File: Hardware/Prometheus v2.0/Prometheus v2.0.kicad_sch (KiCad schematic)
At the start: 21 parts, among them K1 Relay_SPDT, Q1 IRLML6246, Q2 IRLML6246, Q3 IRLML6246, SW1 SW_Push, U1 LMS1585ACT-3.3_NOPB, U2 LM7805_TO220

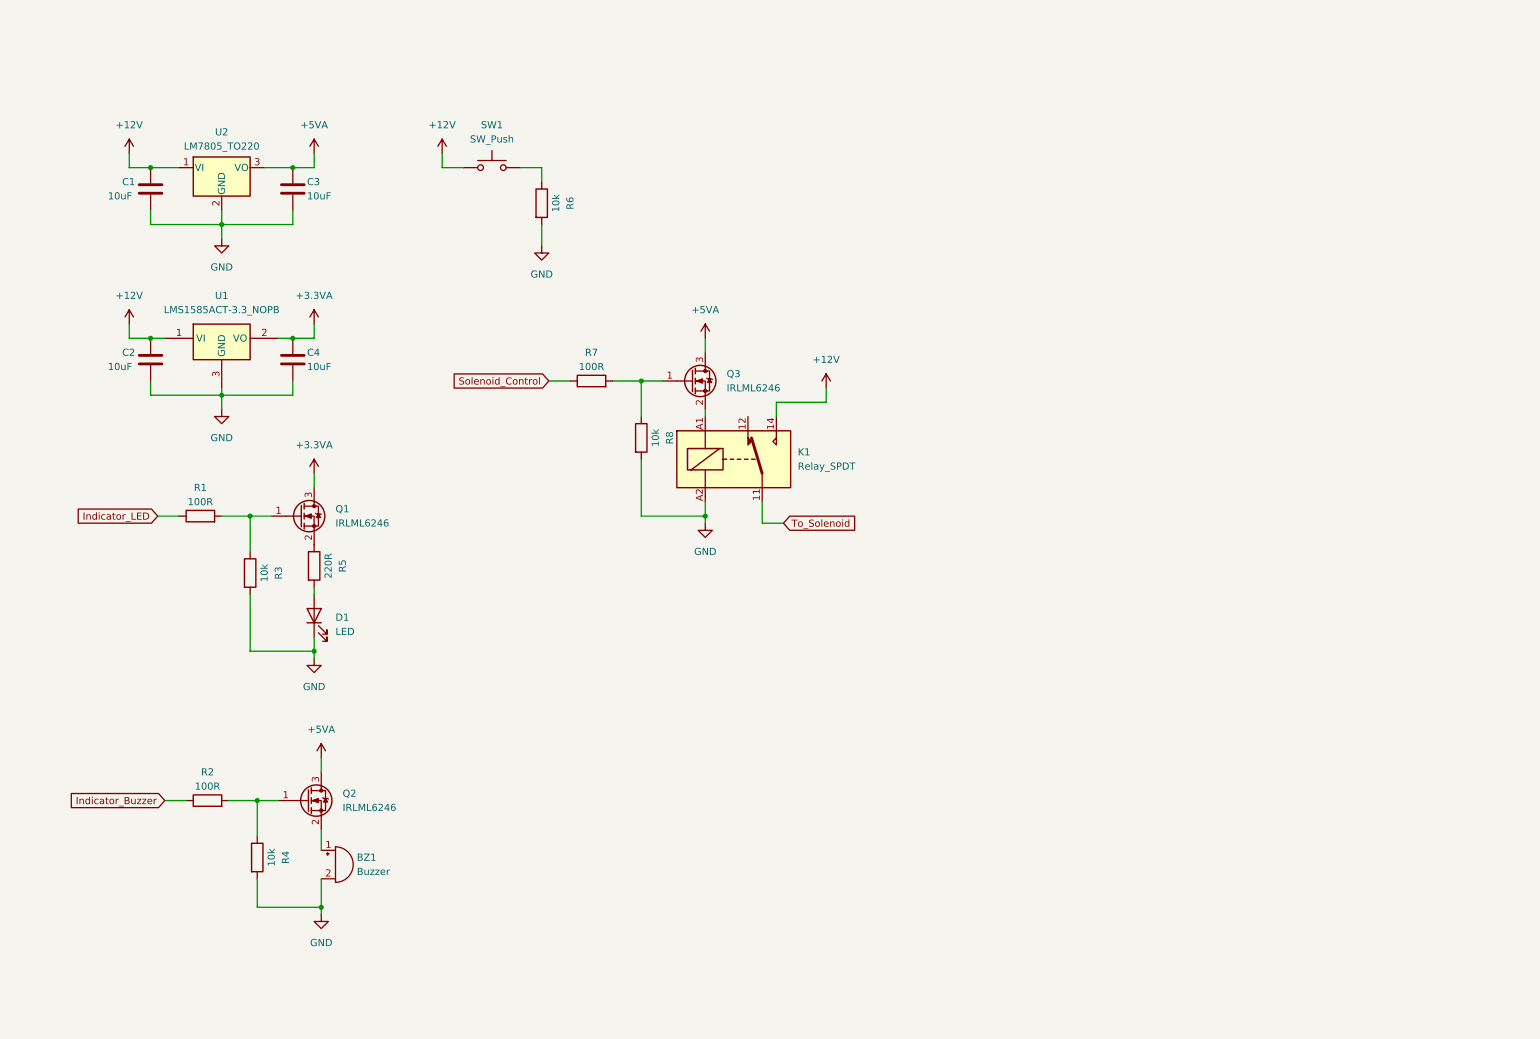
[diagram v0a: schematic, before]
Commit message: v1.0 - Phase 2
- Completed the complete schematic
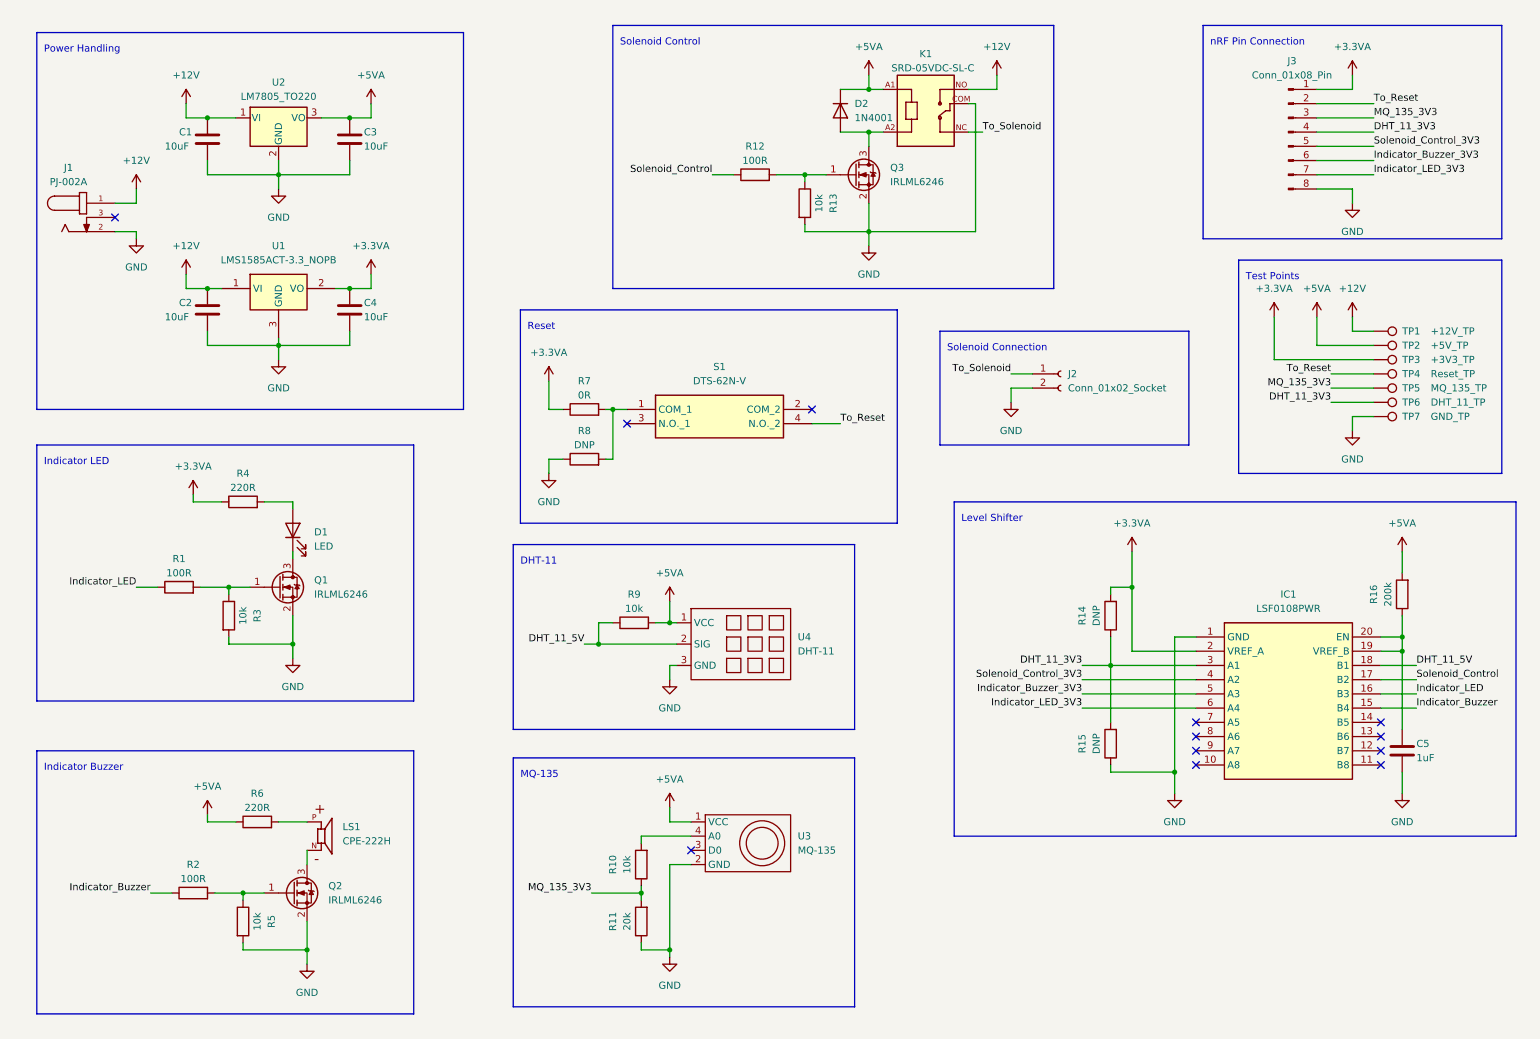
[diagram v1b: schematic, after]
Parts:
- removed BZ1: Buzzer, symbol Device:Buzzer
- removed K1: Relay_SPDT, symbol Relay:Relay_SPDT
- removed SW1: SW_Push, symbol Switch:SW_Push
- added C5: 1uF, symbol Device:C
- added D2: 1N4001, Diode_THT:D_DO-41_SOD81_P10.16mm_Horizontal, symbol Diode:1N4001
- added IC1: LSF0108PWR, SOP65P640X120-20N, symbol Level Shifter:LSF0108PWR
- added J1: PJ-002A, PJ-002A:CUI_PJ-002A, symbol Connectors:PJ-002A
- added J2: Conn_01x02_Socket, symbol Connector:Conn_01x02_Socket
- added J3: Conn_01x08_Pin, symbol Connector:Conn_01x08_Pin
- added K1: SRD-05VDC-SL-C, SRD-05VDC-SL-C:RELAY_SRD-05VDC-SL-C, symbol Mechanical Relays:SRD-05VDC-SL-C
- added LS1: CPE-222H, CPE-222H:CUI_CPE-222H, symbol Piezzo Electric Buzzer:CPE-222H
- added R10, R9: 10k, symbol Device:R
- added R11: 20k, symbol Device:R
- added R14, R15, R8: DNP, symbol Device:R
- added R16: 200k, symbol Device:R
- added R7: 0R, symbol Device:R
- added S1: DTS-62N-V, DTS62NV, symbol Tactile Switch:DTS-62N-V
- added TP1: +12V_TP, symbol Connector:TestPoint
- added TP2: +5V_TP, symbol Connector:TestPoint
- added TP3: +3V3_TP, symbol Connector:TestPoint
- added TP4: Reset_TP, symbol Connector:TestPoint
- added TP5: MQ_135_TP, symbol Connector:TestPoint
- added TP6: DHT_11_TP, symbol Connector:TestPoint
- added TP7: GND_TP, symbol Connector:TestPoint
- added U3: MQ-135, symbol Sensors:MQ-135
- added U4: DHT-11, symbol Sensors:DHT-11
- R4, R6: value 10k -> 220R
- R5: value 220R -> 10k
- renumbered R7 to R12, R8 to R13
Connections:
- net +12V: now also J1.1, K1.NO, TP1.1
- net +3.3VA: now also R4.1, IC1.2 (VREF_A), J3.1 (Pin_1), R14.2, R7.1, TP3.1; no longer Q1.3 (D)
- net +5VA: now also R6.1, D2.1 (K), K1.A1, R16.2, R9.2, TP2.1, U3.1 (VCC), U4.1 (VCC); no longer Q2.3 (D), Q3.3 (D)
- net GND: now also Q1.2 (S), Q2.2 (S), Q3.2 (S), R5.2, C5.2, IC1.1 (GND), J1.2, J2.2 (Pin_2), J3.8 (Pin_8), K1.COM, R11.1, R15.1, R8.1, TP7.1, U3.2 (GND), U4.3 (GND); no longer D1.1 (K), R4.2, R6.2
- net Indicator_Buzzer: now also IC1.15 (B4)
- net Indicator_LED: now also IC1.16 (B3)
- net Solenoid_Control: now also IC1.17 (B2)
- net To_Solenoid: now also J2.1 (Pin_1), K1.NC
- net at R5.1: now also Q2.1 (G), R2.2; no longer Q1.2 (S)
- net at D1.2 (A): now also R4.2; no longer R5.2
- new net: LS1.N, Q2.3 (D)
- new net: LS1.P, R6.2
- new net: R7.2, R8.2, S1.1 (COM_1)
- new net: D1.1 (K), Q1.3 (D)
- new net: D2.2 (A), K1.A2, Q3.3 (D)
- new net: C5.1, IC1.19 (VREF_B), IC1.20 (EN), R16.1
- new net: R10.2, U3.4 (A0)
- new net DHT_11_3V3: IC1.3 (A1), J3.4 (Pin_4), R14.1, R15.2, TP6.1
- new net DHT_11_5V: IC1.18 (B1), R9.1, U4.2 (SIG)
- new net Indicator_Buzzer_3V3: IC1.5 (A3), J3.6 (Pin_6)
- new net Indicator_LED_3V3: IC1.6 (A4), J3.7 (Pin_7)
- new net MQ_135_3V3: J3.3 (Pin_3), R10.1, R11.2, TP5.1
- new net Solenoid_Control_3V3: IC1.4 (A2), J3.5 (Pin_5)
- new net To_Reset: J3.2 (Pin_2), S1.4 (N.O._2), TP4.1
- no-connect marks 0 -> 12
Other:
- note added: "DHT-11"
- note added: "Indicator Buzzer"
- note added: "Indicator LED"
- note added: "Level Shifter"
- note added: "MQ-135"
- note added: "Power Handling"
- note added: "Reset"
- note added: "Solenoid Connection"
- note added: "Solenoid Control"
- note added: "Test Points"
- note added: "nRF Pin Connection"
- company: (none) -> Asanka Sovis
- title: (none) -> Prometheus Main PCB v2.0
- moved on the sheet: C1, C2, C3, C4, Q1, Q3, R1, R12, R13, R3, U1, U2

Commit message: v2.1
- First design completion
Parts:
- removed C5: 1uF, symbol Device:C
- removed J3: Conn_01x08_Pin, symbol Connector:Conn_01x08_Pin
- removed R11: 20k, symbol Device:R
- removed R16: 200k, symbol Device:R
- removed R9: 10k, symbol Device:R
- removed TP1: +12V_TP, symbol Connector:TestPoint
- removed TP2: +5V_TP, symbol Connector:TestPoint
- removed TP3: +3V3_TP, symbol Connector:TestPoint
- removed TP4: Reset_TP, symbol Connector:TestPoint
- removed TP5: MQ_135_TP, symbol Connector:TestPoint
- removed TP6: DHT_11_TP, symbol Connector:TestPoint
- removed TP7: GND_TP, symbol Connector:TestPoint
- removed U3: MQ-135, symbol Sensors:MQ-135
- removed U4: DHT-11, symbol Sensors:DHT-11
- added C3, C7: 0.1uF, Capacitor_SMD:C_0805_2012Metric, symbol Device:C
- added C6: 1uF, Capacitor_SMD:C_0805_2012Metric, symbol Device:C
- added J3: Conn_01x12_Pin, Connector_PinHeader_2.54mm:PinHeader_1x12_P2.54mm_Horizontal, symbol Connector:Conn_01x12_Pin
- added R12, R2, R21: 10k, Resistor_SMD:R_0805_2012Metric, symbol Device:R
- added R3: 20k, Resistor_SMD:R_0805_2012Metric, symbol Device:R
- added R5, R6: DNP, Resistor_SMD:R_0805_2012Metric, symbol Device:R
- added R7: 2k, Resistor_SMD:R_0805_2012Metric, symbol Device:R
- added R8: 200k, Resistor_SMD:R_0805_2012Metric, symbol Device:R
- added TP1: 12V_TP, TestPoint:TestPoint_Pad_1.0x1.0mm, symbol Connector:TestPoint_Small
- added TP10: MQ_135_SDA_TP, TestPoint:TestPoint_Pad_1.0x1.0mm, symbol Connector:TestPoint_Small
- added TP11: MQ_135_5V_TP, TestPoint:TestPoint_Pad_1.0x1.0mm, symbol Connector:TestPoint_Small
- added TP12: MQ_135_D_TP, TestPoint:TestPoint_Pad_1.0x1.0mm, symbol Connector:TestPoint_Small
- added TP13: Solenoid_Out_TP, TestPoint:TestPoint_Pad_1.0x1.0mm, symbol Connector:TestPoint_Small
- added TP14: LED_TP, TestPoint:TestPoint_Pad_1.0x1.0mm, symbol Connector:TestPoint_Small
- added TP15: Buzzer_TP, TestPoint:TestPoint_Pad_1.0x1.0mm, symbol Connector:TestPoint_Small
- added TP16: Solenoid_Control_3V3_TP, TestPoint:TestPoint_Pad_1.0x1.0mm, symbol Connector:TestPoint_Small
- added TP17: Indicator_Buzzer_3V3_TP, TestPoint:TestPoint_Pad_1.0x1.0mm, symbol Connector:TestPoint_Small
- added TP18: Indicator_LED_3V3_TP, TestPoint:TestPoint_Pad_1.0x1.0mm, symbol Connector:TestPoint_Small
- added TP19: DHT_11_3V3_TP, TestPoint:TestPoint_Pad_1.0x1.0mm, symbol Connector:TestPoint_Small
- added TP2: MQ_135_A_3V3_TP, TestPoint:TestPoint_Pad_1.0x1.0mm, symbol Connector:TestPoint_Small
- added TP20: MQ_135_SDA_3V3_TP, TestPoint:TestPoint_Pad_1.0x1.0mm, symbol Connector:TestPoint_Small
- added TP21: MQ_135_SCL_3V3_TP, TestPoint:TestPoint_Pad_1.0x1.0mm, symbol Connector:TestPoint_Small
- added TP22: MQ_135_CS_3V3_TP, TestPoint:TestPoint_Pad_1.0x1.0mm, symbol Connector:TestPoint_Small
- added TP23: MQ_135_D_3V3_TP, TestPoint:TestPoint_Pad_1.0x1.0mm, symbol Connector:TestPoint_Small
- added TP24: GND_TP, TestPoint:TestPoint_Pad_2.0x2.0mm, symbol Connector:TestPoint_Small
- added TP25: DHT_11_TP, TestPoint:TestPoint_Pad_1.0x1.0mm, symbol Connector:TestPoint_Small
- added TP26: Reset_TP, TestPoint:TestPoint_Pad_1.0x1.0mm, symbol Connector:TestPoint_Small
- added TP3: VREF_A_TP, TestPoint:TestPoint_Pad_1.0x1.0mm, symbol Connector:TestPoint_Small
- added TP4: 5V_TP, TestPoint:TestPoint_Pad_1.0x1.0mm, symbol Connector:TestPoint_Small
- added TP5: 3V3_TP, TestPoint:TestPoint_Pad_1.0x1.0mm, symbol Connector:TestPoint_Small
- added TP6: VREF_B_TP, TestPoint:TestPoint_Pad_1.0x1.0mm, symbol Connector:TestPoint_Small
- added TP7: MQ_135_SCL_TP, TestPoint:TestPoint_Pad_1.0x1.0mm, symbol Connector:TestPoint_Small
- added TP8: MQ_135_CS_TP, TestPoint:TestPoint_Pad_1.0x1.0mm, symbol Connector:TestPoint_Small
- added TP9: Solenoid_In_TP, TestPoint:TestPoint_Pad_1.0x1.0mm, symbol Connector:TestPoint_Small
- added U3: XD549, Package_DIP:DIP-8_W7.62mm, symbol ADC:XD549
- added U4: MQ-135, symbol Sensors:MQ-135
- added U5: DHT-11, symbol Sensors:DHT-11
- C1, C2: footprint (none) -> Capacitor_SMD:C_0805_2012Metric; JLCPCB (none) -> https://jlcpcb.com/partdetail/Yageo-CC0805KKX5R6BB106/C89832
- C4: renamed from C3; footprint (none) -> Capacitor_SMD:C_0805_2012Metric; JLCPCB (none) -> https://jlcpcb.com/partdetail/Yageo-CC0805KKX5R6BB106/C89832
- C5: renamed from C4; footprint (none) -> Capacitor_SMD:C_0805_2012Metric; JLCPCB (none) -> https://jlcpcb.com/partdetail/Yageo-CC0805KKX5R6BB106/C89832
- D1: renamed from D2; JLCPCB (none) -> https://jlcpcb.com/partdetail/VishayIntertech-1N4001_E373/C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
- D2: renamed from D1; footprint (none) -> LED_THT:LED_D3.0mm_FlatTop; JLCPCB (none) -> https://jlcpcb.com/partdetail/EverlightElec-333_2SURD_S530_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
- IC1: JLCPCB (none) -> https://jlcpcb.com/partdetail/Nexperia-LSF0108PWQ100J/C5515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
- J1: JLCPCB (none) -> https://jlcpcb.com/partdetail/Jinjia-DC02IB/C718035
- K1: JLCPCB (none) -> https://jlcpcb.com/partdetail/Ningbo_SongleRelay-SRA_05VDCC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
- LS1: footprint CPE-222H:CUI_CPE-222H -> Buzzer_Beeper:MagneticBuzzer_StarMicronics_HMB-06_HMB-12; JLCPCB (none) -> https://jlcpcb.com/partdetail/Jiangsu_HuanengElec-HMB120605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
- Q1: renamed from Q3; JLCPCB (none) -> https://jlcpcb.com/partdetail/InfineonTechnologies-IRLML624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
- Q2: renamed from Q1; JLCPCB (none) -> https://jlcpcb.com/partdetail/InfineonTechnologies-IRLML624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
- Q3: renamed from Q2; JLCPCB (none) -> https://jlcpcb.com/partdetail/InfineonTechnologies-IRLML624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
- R1: renamed from R15; footprint (none) -> Resistor_SMD:R_0805_2012Metric
- R10: value 10k -> 100R; footprint (none) -> Resistor_SMD:R_0805_2012Metric; JLCPCB (none) -> https://jlcpcb.com/partdetail/Yageo-AC0805JR7W100RL/C728002
- R11: renamed from R13; footprint (none) -> Resistor_SMD:R_0805_2012Metric; JLCPCB (none) -> https://jlcpcb.com/partdetail/Yageo-AC0805JR0710KL/C138260
- R13: renamed from R1; footprint (none) -> Resistor_SMD:R_0805_2012Metric; JLCPCB (none) -> https://jlcpcb.com/partdetail/Yageo-AC0805JR7W100RL/C728002
- R14: renamed from R3; footprint (none) -> Resistor_SMD:R_0805_2012Metric; JLCPCB (none) -> https://jlcpcb.com/partdetail/Yageo-AC0805JR0710KL/C138260
- R15: renamed from R4; footprint (none) -> Resistor_SMD:R_0805_2012Metric; JLCPCB (none) -> https://jlcpcb.com/partdetail/Kamaya-RPCH20K221JTP/C340559
- R16: renamed from R2; footprint (none) -> Resistor_SMD:R_0805_2012Metric; JLCPCB (none) -> https://jlcpcb.com/partdetail/Yageo-AC0805JR7W100RL/C728002
- R17: renamed from R5; footprint (none) -> Resistor_SMD:R_0805_2012Metric; JLCPCB (none) -> https://jlcpcb.com/partdetail/Yageo-AC0805JR0710KL/C138260
- R18: renamed from R6; footprint (none) -> Resistor_SMD:R_0805_2012Metric; JLCPCB (none) -> https://jlcpcb.com/partdetail/Kamaya-RPCH20K221JTP/C340559
- R19: renamed from R7; value 0R -> 100R; footprint (none) -> Resistor_SMD:R_0805_2012Metric; JLCPCB (none) -> https://jlcpcb.com/partdetail/Yageo-AC0805JR7W100RL/C728002
- R20: renamed from R8; footprint (none) -> Resistor_SMD:R_0805_2012Metric
- R4: renamed from R14; footprint (none) -> Resistor_SMD:R_0805_2012Metric
- R9: renamed from R12; footprint (none) -> Resistor_SMD:R_0805_2012Metric; JLCPCB (none) -> https://jlcpcb.com/partdetail/Yageo-AC0805JR7W100RL/C728002
- S1: JLCPCB (none) -> https://jlcpcb.com/partdetail/Diptronics-DTSA_65NV/C224975
- U1: JLCPCB (none) -> https://jlcpcb.com/partdetail/TexasInstruments-LMS1585ACT_3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
- U2: JLCPCB (none) -> https://jlcpcb.com/partdetail/6334298-LM7805CT/C5444281
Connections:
- net MQ_135_3V3 is gone; now on net MQ_135_SDA: R10.1
- net +12V: now also TP1.1
- net DHT_11_3V3: now also R1.1, R4.2, J3.4 (Pin_4), TP19.1; no longer R1.2, R4.1
- net DHT_11_5V: now also R21.1, TP25.1, U5.2 (SIG)
- net GND: now also R1.2, C3.1, C6.2, C7.2, J3.12 (Pin_12), R3.1, TP24.1, U3.4 (GND), U4.2 (GND), U5.3 (GND); no longer K1.COM, R1.1
- net Indicator_Buzzer: now also IC1.16 (B3); no longer IC1.15 (B4)
- net Indicator_Buzzer_3V3: now also J3.6 (Pin_6), TP17.1
- net Indicator_LED: now also IC1.15 (B4); no longer IC1.16 (B3)
- net Indicator_LED_3V3: now also J3.7 (Pin_7), TP18.1
- net Solenoid_Control_3V3: now also J3.5 (Pin_5), TP16.1
- net To_Reset: now also S1.3 (N.O._1), J3.2 (Pin_2), TP26.1
- net To_Solenoid: now also K1.COM, TP13.1; no longer K1.NC
- net at R19.2, R20.2, S1.1 (COM_1): now also S1.2 (COM_2)
- net at Q2.1 (G), R13.2, R14.1: now also TP14.1
- net at Q3.1 (G), R16.2, R17.1: now also TP15.1
- net at Q1.1 (G), R11.1, R9.2: now also TP9.1
- net VREF_B: now reaches IC1.19 (VREF_B), IC1.20 (EN)
- net VREF_B: now also C6.1, R8.2, TP6.1
- net MQ_135_D_3V3: now reaches IC1.10 (A8)
- net MQ_135_D_3V3: now also J3.11 (Pin_11), TP23.1
- net MQ_135_D: now reaches IC1.11 (B8)
- net MQ_135_D: now also TP12.1, U4.3 (D0)
- net MQ_135_CS: now reaches IC1.12 (B7)
- net MQ_135_CS: now also TP8.1, U3.5 (CS)
- net MQ_135_SCL: now reaches IC1.13 (B6)
- net MQ_135_SCL: now also TP7.1, U3.7 (CLK)
- net MQ_135_SDA: now reaches IC1.14 (B5)
- net MQ_135_SDA: now also R12.2, TP10.1
- net MQ_135_SDA_3V3: now reaches IC1.7 (A5)
- net MQ_135_SDA_3V3: now also J3.8 (Pin_8), TP20.1
- net MQ_135_SCL_3V3: now reaches IC1.8 (A6)
- net MQ_135_SCL_3V3: now also J3.9 (Pin_9), R6.2, TP21.1
- net MQ_135_CS_3V3: now reaches IC1.9 (A7)
- net MQ_135_CS_3V3: now also J3.10 (Pin_10), R5.2, TP22.1
- net at R10.2: now also U3.6 (SDA)
- net +3.3VA renamed +3.3V
- net +3.3V: now also R4.1, J3.1 (Pin_1), R5.1, R6.1, TP3.1, TP5.1; no longer R15.1, R4.2
- net +5VA renamed +5V
- net +5V: now also R15.1, C7.1, R12.1, R21.2, R8.1, TP4.1, U3.1 (REF+), U3.8 (VCC), U4.1 (VCC), U5.1 (VCC)
- new net: R7.1, U3.3 (REF-)
- new net: C3.2, R7.2
- new net MQ_135_A: R2.1, TP11.1, U3.2 (A0), U4.4 (A0)
- new net MQ_135_A_3V3: J3.3 (Pin_3), R2.2, R3.2, TP2.1
- no-connect marks 12 -> 2
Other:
- note added: "MQ-135 ADC"
- note added: "MQ-135 Level Shifter"
- note added: "Testpoints"
- note removed: "Test Points"
- moved on the sheet: C1, C2, C4, C5, D1, D2, IC1, J1, J2, K1, LS1, Q1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

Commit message: v2.2
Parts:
- removed C6: 1uF, Capacitor_SMD:C_0805_2012Metric, symbol Device:C
- removed IC1: LSF0108PWR, SOP65P640X120-20N, symbol Level Shifter:LSF0108PWR
- removed J1: PJ-002A, PJ-002A:CUI_PJ-002A, symbol Connectors:PJ-002A
- removed J3: Conn_01x12_Pin, Connector_PinHeader_2.54mm:PinHeader_1x12_P2.54mm_Horizontal, symbol Connector:Conn_01x12_Pin
- removed R8: 200k, Resistor_SMD:R_0805_2012Metric, symbol Device:R
- added H1, H2, H3, H4: MountingHole, MountingHole:MountingHole_2.5mm_Pad_TopBottom, symbol Mechanical:MountingHole
- added IC1: TXS0108EQPWRQ1, TXS0108EQPWRQ1:SOP65P640X120-20N, symbol Level Shifter:TXS0108EQPWRQ1
- added J1: DC-005-5A-2.0, Connectors:XKB_DC-005-5A-2.0, symbol Connectors:DC-005-5A-2.0
- added J3: Conn_01x13_Pin, Connector_PinHeader_2.54mm:PinHeader_1x13_P2.54mm_Vertical, symbol Connector:Conn_01x13_Pin
- added R7: 10k, Resistor_SMD:R_0805_2012Metric, symbol Device:R
- added TP9: VREF_B_TP, TestPoint:TestPoint_Pad_1.0x1.0mm, symbol Connector:TestPoint_Small
- J2: footprint (none) -> Connector_Molex:Molex_Mega-Fit_76825-0002_2x01_P5.70mm_Horizontal
- S1: footprint DTS62NV -> DTS-62N-V:DTS62NV
- TP6: value VREF_B_TP -> LS_EN_TP
- U1: footprint TO254P470X1028X1955-3P -> LMS1585ACT-3.3_NOPB:TO254P470X1028X1955-3P
- U4: footprint (none) -> Sensors:MQ-135
- U5: footprint (none) -> Sensors:DHT-11
- renumbered C7 to C6, R5 to R2, R2 to R3, R3 to R4, R4 to R5, R7 to R8, TP9 to TP10, TP10 to TP11, TP11 to TP12, TP12 to TP13, TP13 to TP14, TP14 to TP15, TP15 to TP16, TP16 to TP17, TP17 to TP18, TP18 to TP19, TP19 to TP20, TP20 to TP21, TP21 to TP22, TP22 to TP23, TP23 to TP24, TP24 to TP25, TP25 to TP26, TP26 to TP27
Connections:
- net +12V: now also J1.1
- net +3.3V: now also IC1.2 (VCCA), J3.1 (Pin_1)
- net +5V: now also U5.2 (VCC), IC1.19 (VCCB), TP9.1; no longer U5.1 (VCC)
- net DHT_11_3V3: now also IC1.1 (A1), J3.4 (Pin_4)
- net DHT_11_5V: now also U5.1 (SIG), IC1.20 (B1); no longer U5.2 (SIG)
- net GND: now also IC1.11 (GND), J1.2, J3.13 (Pin_13), R7.2
- net Indicator_Buzzer: now also IC1.17 (B3)
- net Indicator_Buzzer_3V3: now also IC1.4 (A3), J3.6 (Pin_6)
- net Indicator_LED: now also IC1.16 (B4)
- net Indicator_LED_3V3: now also IC1.5 (A4), J3.7 (Pin_7)
- net MQ_135_A_3V3: now also J3.3 (Pin_3)
- net MQ_135_CS: now also IC1.13 (B7)
- net MQ_135_CS_3V3: now also IC1.8 (A7), J3.10 (Pin_10)
- net MQ_135_D: now also IC1.12 (B8)
- net MQ_135_D_3V3: now also IC1.9 (A8), J3.11 (Pin_11)
- net MQ_135_SCL: now also IC1.14 (B6)
- net MQ_135_SCL_3V3: now also IC1.7 (A6), J3.9 (Pin_9)
- net MQ_135_SDA: now also IC1.15 (B5)
- net MQ_135_SDA_3V3: now also IC1.6 (A5), J3.8 (Pin_8)
- net Solenoid_Control: now also IC1.18 (B2)
- net Solenoid_Control_3V3: now also IC1.3 (A2), J3.5 (Pin_5)
- net To_Reset: now also J3.2 (Pin_2)
- net at Q3.3 (D): now also LS1.2; no longer LS1.N
- net at R18.2: now also LS1.1; no longer LS1.P
- net VREF_B renamed LS_EN
- net LS_EN: now also IC1.10 (OE), J3.12 (Pin_12), R7.1
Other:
- title: Prometheus Main PCB v2.0 -> Prometheus Main PCB v2.3
- moved on the sheet: R2, R6
